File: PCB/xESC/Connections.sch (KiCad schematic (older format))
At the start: 1 part

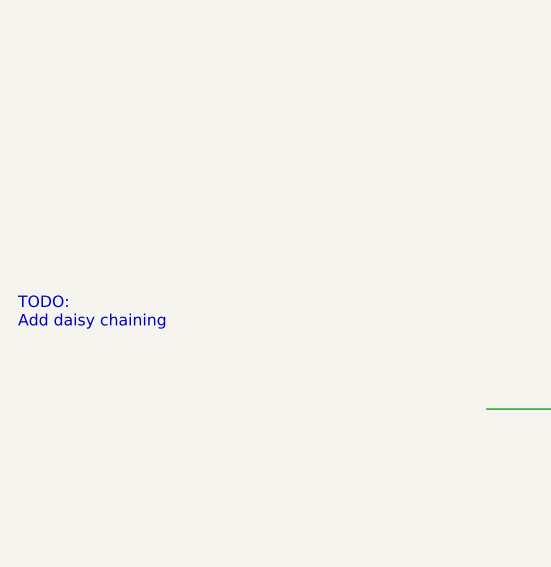
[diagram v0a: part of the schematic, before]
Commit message: added missing connection
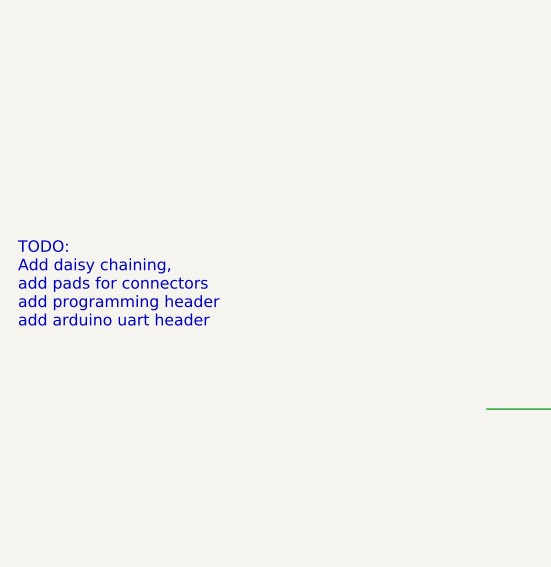
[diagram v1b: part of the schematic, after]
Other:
- note added: "TODO:\nAdd daisy chaining,\nadd pads for connectors\nadd programming header\nadd arduino uart header"
- note removed: "TODO:\nAdd daisy chaining"
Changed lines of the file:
@@
 RXD
 Text Notes 2100 3000 0    50   ~ 0
-TODO:\nAdd daisy chaining
+TODO:\nAdd daisy chaining,\nadd pads for connectors\nadd programming header\nadd arduino uart header
 Text HLabel 5750 3650 2    50   Output ~ 0
 INPUT

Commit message: wip
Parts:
- gave numbers to parts that had none: 1
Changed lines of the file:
@@
 VCCIO
 $Comp
-L Device:R R?
+L Device:R R16
 U 1 1 61826336
 P 5000 3200
-F 0 "R?" V 5207 3200 50  0000 C CNN
+F 0 "R16" V 5207 3200 50  0000 C CNN
 F 1 "1kR" V 5116 3200 50  0000 C CNN
 F 2 "Resistor_SMD:R_0805_2012Metric_Pad1.20x1.40mm_HandSolder" V 4930 3200 50  0001 C CNN

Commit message: wip
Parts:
- added J1: Conn_01x05_Male, Connector_PinHeader_2.54mm:PinHeader_1x05_P2.54mm_Vertical, symbol Connector:Conn_01x05_Male
- added J2, J3: Conn_01x03_Male, Connector_PinHeader_2.54mm:PinHeader_1x03_P2.54mm_Vertical, symbol Connector:Conn_01x03_Male
- added R? (x2): 1kR, Resistor_SMD:R_0805_2012Metric_Pad1.20x1.40mm_HandSolder, symbol Device:R
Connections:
- net labels added: INPUT_ANALOG, INPUT_PWM
- net labels removed: INPUT
- wire segments 3 -> 38
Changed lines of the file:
@@
 Text HLabel 5750 1800 2    50   UnSpc ~ 0
 GND
-Text HLabel 5750 2250 2    50   Input ~ 0
+Text HLabel 5750 2850 2    50   Input ~ 0
 HALL_V+
 Text HLabel 5750 2400 2    50   Output ~ 0
@@
 TODO:\nAdd daisy chaining,\nadd pads for connectors\nadd programming header\nadd arduino uart header
 Text HLabel 5750 3650 2    50   Output ~ 0
-INPUT
+INPUT_PWM
 Text HLabel 5750 4000 2    50   Input ~ 0
 U
@@
 Text HLabel 5750 5250 2    50   Input ~ 0
 SCK
+$Comp
+L Connector:Conn_01x05_Male J1
+U 1 1 61B78D2B
+P 4950 2450
+F 0 "J1" H 5058 2831 50  0000 C CNN
+F 1 "Conn_01x05_Male" H 5058 2740 50  0000 C CNN
+F 2 "Connector_PinHeader_2.54mm:PinHeader_1x05_P2.54mm_Vertical" H 4950 2450 50  0001 C CNN
+F 3 "~" H 4950 2450 50  0001 C CNN
+	1    4950 2450
+	1    0    0    -1
+$EndComp
+Wire Wire Line
+	5750 1800 5600 1800
+Wire Wire Line
+	5600 2250 5150 2250
+Wire Wire Line
+	5450 2400 5450 2350
+Wire Wire Line
+	5450 2350 5150 2350
+Wire Wire Line
+	5400 2550 5400 2450
+Wire Wire Line
+	5400 2450 5150 2450
+Wire Wire Line
+	5350 2700 5350 2550
+Wire Wire Line
+	5350 2550 5150 2550
+Wire Wire Line
+	5250 2850 5250 2650
+Wire Wire Line
+	5250 2650 5150 2650
+Wire Wire Line
+	5750 2850 5250 2850
+Wire Wire Line
+	5750 2700 5350 2700
+Wire Wire Line
+	5750 2550 5400 2550
+Wire Wire Line
+	5750 2400 5450 2400
+Wire Wire Line
+	5600 1800 5600 2250
+Text HLabel 5750 3750 2    50   Output ~ 0
+INPUT_ANALOG
+$Comp
+L Connector:Conn_01x03_Male J2
+U 1 1 61BD29C1
+P 3550 3750
+F 0 "J2" H 3658 4031 50  0000 C CNN
+F 1 "Conn_01x03_Male" H 3658 3940 50  0000 C CNN
+F 2 "Connector_PinHeader_2.54mm:PinHeader_1x03_P2.54mm_Vertical" H 3550 3750 50  0001 C CNN
+F 3 "~" H 3550 3750 50  0001 C CNN
+	1    3550 3750
+	1    0    0    -1
+$EndComp
+$Comp
+L Connector:Conn_01x03_Male J3
+U 1 1 61BD440A
+P 3550 4250
+F 0 "J3" H 3658 4531 50  0000 C CNN
+F 1 "Conn_01x03_Male" H 3658 4440 50  0000 C CNN
+F 2 "Connector_PinHeader_2.54mm:PinHeader_1x03_P2.54mm_Vertical" H 3550 4250 50  0001 C CNN
+F 3 "~" H 3550 4250 50  0001 C CNN
+	1    3550 4250
+	1    0    0    -1
+$EndComp
+$Comp
+L power:GND #PWR0117
+U 1 1 61BD4BA0
+P 5600 2250
+F 0 "#PWR0117" H 5600 2000 50  0001 C CNN
+F 1 "GND" H 5605 2077 50  0000 C CNN
+F 2 "" H 5600 2250 50  0001 C CNN
+F 3 "" H 5600 2250 50  0001 C CNN
+	1    5600 2250
+	1    0    0    -1
+$EndComp
+Connection ~ 5600 2250
+Wire Wire Line
+	3750 3650 3950 3650
+Wire Wire Line
+	3950 3650 3950 4150
+Wire Wire Line
+	3750 4150 3950 4150
+Connection ~ 3950 4150
+Wire Wire Line
+	3950 4150 3950 4650
+Wire Wire Line
+	3750 4250 4050 4250
+Wire Wire Line
+	4050 4250 4050 3750
+Wire Wire Line
+	3750 3750 4050 3750
+Connection ~ 4050 3750
+Wire Wire Line
+	5750 1500 4050 1500
+Wire Wire Line
+	4050 1500 4050 3750
+Wire Wire Line
+	3750 3850 5150 3850
+Wire Wire Line
+	5150 3850 5150 3650
+Wire Wire Line
+	5150 3650 5750 3650
+Wire Wire Line
+	5750 3750 5250 3750
+Wire Wire Line
+	5250 3750 5250 4150
+Wire Wire Line
+	5250 4350 3750 4350
+$Comp
+L power:GND #PWR0118
+U 1 1 61BD88B8
+P 3950 4650
+F 0 "#PWR0118" H 3950 4400 50  0001 C CNN
+F 1 "GND" H 3955 4477 50  0000 C CNN
+F 2 "" H 3950 4650 50  0001 C CNN
+F 3 "" H 3950 4650 50  0001 C CNN
+	1    3950 4650
+	1    0    0    -1
+$EndComp
+$Comp
+L Device:R R?
+U 1 1 61BF443C
+P 4900 3650
+F 0 "R?" V 5107 3650 50  0000 C CNN
+F 1 "1kR" V 5016 3650 50  0000 C CNN
+F 2 "Resistor_SMD:R_0805_2012Metric_Pad1.20x1.40mm_HandSolder" V 4830 3650 50  0001 C CNN
+F 3 "~" H 4900 3650 50  0001 C CNN
+	1    4900 3650
+	0    1    1    0
+$EndComp
+$Comp
+L Device:R R?
+U 1 1 61BF524C
+P 4900 4150
+F 0 "R?" V 5107 4150 50  0000 C CNN
+F 1 "1kR" V 5016 4150 50  0000 C CNN
+F 2 "Resistor_SMD:R_0805_2012Metric_Pad1.20x1.40mm_HandSolder" V 4830 4150 50  0001 C CNN
+F 3 "~" H 4900 4150 50  0001 C CNN
+	1    4900 4150
+	0    1    1    0
+$EndComp
+Wire Wire Line
+	5150 3650 5050 3650
+Connection ~ 5150 3650
+Wire Wire Line
+	5050 4150 5250 4150
+Connection ~ 5250 4150
+Wire Wire Line
+	5250 4150 5250 4350
+Wire Wire Line
+	4750 4150 3950 4150
+Wire Wire Line
+	4750 3650 3950 3650
+Connection ~ 3950 3650
 $EndSCHEMATC

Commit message: wip
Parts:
- added J4: Conn_01x03_Male, Connector_PinHeader_2.54mm:PinHeader_1x03_P2.54mm_Vertical, symbol Connector:Conn_01x03_Male
- added TP1, TP2, TP3, TP4, TP5, TP6, TP7, TP?: TestPoint, xESC:TestPoint_Pad_1.5x1.5mm, symbol Connector:TestPoint
- gave numbers to parts that had none: 2
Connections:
- net labels added: SS_EXT_SPI
- net labels removed: HALL_V+
- wire segments 38 -> 50
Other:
- note added: "Phase is connected using\nmanually placed solder pads"
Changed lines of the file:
@@
 Comment4 ""
 $EndDescr
-Text HLabel 5750 1650 2    50   Output ~ 0
+Text HLabel 7700 5400 2    50   Output ~ 0
 V_IN
 Text HLabel 5750 1800 2    50   UnSpc ~ 0
 GND
-Text HLabel 5750 2850 2    50   Input ~ 0
-HALL_V+
 Text HLabel 5750 2400 2    50   Output ~ 0
 HALL_U
@@
 Text HLabel 5750 3200 2    50   Input ~ 0
 TXD
-Text HLabel 5750 3350 2    50   Output ~ 0
-RXD
 Text Notes 2100 3000 0    50   ~ 0
 TODO:\nAdd daisy chaining,\nadd pads for connectors\nadd programming header\nadd arduino uart header
 Text HLabel 5750 3650 2    50   Output ~ 0
 INPUT_PWM
-Text HLabel 5750 4000 2    50   Input ~ 0
-U
-Text HLabel 5750 4150 2    50   Input ~ 0
-V
-Text HLabel 5750 4300 2    50   Input ~ 0
-W
 Text HLabel 5750 1500 2    50   Input ~ 0
 VCCIO
@@
 Wire Wire Line
 	4850 3200 4600 3200
-Wire Wire Line
-	4150 3350 5750 3350
-Text HLabel 5750 4750 2    50   Input ~ 0
+Text HLabel 4750 5800 2    50   Input ~ 0
 RESET
-Text HLabel 5750 4900 2    50   Input ~ 0
+Text HLabel 4750 5600 2    50   Input ~ 0
 MISO
-Text HLabel 5750 5050 2    50   Input ~ 0
+Text HLabel 4750 5700 2    50   Input ~ 0
 MOSI
-Text HLabel 5750 5250 2    50   Input ~ 0
+Text HLabel 4750 5500 2    50   Input ~ 0
 SCK
 $Comp
@@
 	5250 2650 5150 2650
 Wire Wire Line
-	5750 2850 5250 2850
-Wire Wire Line
 	5750 2700 5350 2700
 Wire Wire Line
@@
 Connection ~ 3950 4150
 Wire Wire Line
-	3950 4150 3950 4650
+	3950 4150 3950 4550
 Wire Wire Line
 	3750 4250 4050 4250
@@
 Wire Wire Line
 	3750 3750 4050 3750
-Connection ~ 4050 3750
-Wire Wire Line
-	5750 1500 4050 1500
-Wire Wire Line
-	4050 1500 4050 3750
 Wire Wire Line
 	3750 3850 5150 3850
@@
 $EndComp
 $Comp
-L Device:R R?
+L Device:R R17
 U 1 1 61BF443C
 P 4900 3650
-F 0 "R?" V 5107 3650 50  0000 C CNN
+F 0 "R17" V 5107 3650 50  0000 C CNN
 F 1 "1kR" V 5016 3650 50  0000 C CNN
 F 2 "Resistor_SMD:R_0805_2012Metric_Pad1.20x1.40mm_HandSolder" V 4830 3650 50  0001 C CNN
@@
 $EndComp
 $Comp
-L Device:R R?
+L Device:R R18
 U 1 1 61BF524C
 P 4900 4150
-F 0 "R?" V 5107 4150 50  0000 C CNN
+F 0 "R18" V 5107 4150 50  0000 C CNN
 F 1 "1kR" V 5016 4150 50  0000 C CNN
 F 2 "Resistor_SMD:R_0805_2012Metric_Pad1.20x1.40mm_HandSolder" V 4830 4150 50  0001 C CNN
@@
 	4750 3650 3950 3650
 Connection ~ 3950 3650
+Wire Wire Line
+	4550 1500 4550 2850
+Wire Wire Line
+	4550 2850 5250 2850
+Connection ~ 4550 1500
+Wire Wire Line
+	4550 1500 4050 1500
+Text HLabel 7700 5850 2    50   Input ~ 0
+W
+Text HLabel 7700 5700 2    50   Input ~ 0
+V
+Text HLabel 7700 5550 2    50   Input ~ 0
+U
+Text Notes 6550 5750 0    50   ~ 0
+Phase is connected using\nmanually placed solder pads
+$Comp
+L Connector:TestPoint TP2
+U 1 1 61D6B8CA
+P 4600 3200
+F 0 "TP2" H 4542 3226 50  0000 R CNN
+F 1 "TestPoint" H 4542 3317 50  0000 R CNN
+F 2 "xESC:TestPoint_Pad_1.5x1.5mm" H 4800 3200 50  0001 C CNN
+F 3 "~" H 4800 3200 50  0001 C CNN
+	1    4600 3200
+	-1   0    0    1
+$EndComp
+$Comp
+L Connector:TestPoint TP6
+U 1 1 61D6DCA6
+P 4500 5800
+F 0 "TP6" H 4558 5918 50  0000 L CNN
+F 1 "TestPoint" H 4558 5827 50  0000 L CNN
+F 2 "xESC:TestPoint_Pad_1.5x1.5mm" H 4700 5800 50  0001 C CNN
+F 3 "~" H 4700 5800 50  0001 C CNN
+	1    4500 5800
+	1    0    0    -1
+$EndComp
+$Comp
+L Connector:TestPoint TP5
+U 1 1 61D6E8CA
+P 4500 5600
+F 0 "TP5" H 4558 5718 50  0000 L CNN
+F 1 "TestPoint" H 4558 5627 50  0000 L CNN
+F 2 "xESC:TestPoint_Pad_1.5x1.5mm" H 4700 5600 50  0001 C CNN
+F 3 "~" H 4700 5600 50  0001 C CNN
+	1    4500 5600
+	1    0    0    -1
+$EndComp
+$Comp
+L Connector:TestPoint TP4
+U 1 1 61D6F700
+P 4400 5700
+F 0 "TP4" H 4458 5818 50  0000 L CNN
+F 1 "TestPoint" H 4458 5727 50  0000 L CNN
+F 2 "xESC:TestPoint_Pad_1.5x1.5mm" H 4600 5700 50  0001 C CNN
+F 3 "~" H 4600 5700 50  0001 C CNN
+	1    4400 5700
+	1    0    0    -1
+$EndComp
+$Comp
+L Connector:TestPoint TP3
+U 1 1 61D70C5B
+P 4400 5500
+F 0 "TP3" H 4458 5618 50  0000 L CNN
+F 1 "TestPoint" H 4458 5527 50  0000 L CNN
+F 2 "xESC:TestPoint_Pad_1.5x1.5mm" H 4600 5500 50  0001 C CNN
+F 3 "~" H 4600 5500 50  0001 C CNN
+	1    4400 5500
+	1    0    0    -1
+$EndComp
+Wire Wire Line
+	4750 5800 4500 5800
+Wire Wire Line
+	4500 5600 4750 5600
+Wire Wire Line
+	4750 5700 4400 5700
+Wire Wire Line
+	4400 5500 4750 5500
+$Comp
+L Connector:TestPoint TP7
+U 1 1 61D76261
+P 3950 4550
+F 0 "TP7" H 4008 4668 50  0000 L CNN
+F 1 "TestPoint" H 4008 4577 50  0000 L CNN
+F 2 "xESC:TestPoint_Pad_1.5x1.5mm" H 4150 4550 50  0001 C CNN
+F 3 "~" H 4150 4550 50  0001 C CNN
+	1    3950 4550
+	0    -1   -1   0
+$EndComp
+Connection ~ 3950 4550
+Wire Wire Line
+	3950 4550 3950 4650
+Wire Wire Line
+	4550 1500 5750 1500
+$Comp
+L Connector:Conn_01x03_Male J4
+U 1 1 61DB3B50
+P 3550 3100
+F 0 "J4" H 3658 3381 50  0000 C CNN
+F 1 "Conn_01x03_Male" H 3658 3290 50  0000 C CNN
+F 2 "Connector_PinHeader_2.54mm:PinHeader_1x03_P2.54mm_Vertical" H 3550 3100 50  0001 C CNN
+F 3 "~" H 3550 3100 50  0001 C CNN
+	1    3550 3100
+	1    0    0    -1
+$EndComp
+Connection ~ 4050 3750
+$Comp
+L Connector:TestPoint TP1
+U 1 1 61D6C509
+P 4150 3100
+F 0 "TP1" H 4208 3218 50  0000 L CNN
+F 1 "TestPoint" H 4208 3127 50  0000 L CNN
+F 2 "xESC:TestPoint_Pad_1.5x1.5mm" H 4350 3100 50  0001 C CNN
+F 3 "~" H 4350 3100 50  0001 C CNN
+	1    4150 3100
+	1    0    0    -1
+$EndComp
+Wire Wire Line
+	4050 1500 4050 3750
+Wire Wire Line
+	4150 3100 5750 3100
+Text HLabel 5750 3100 2    50   Output ~ 0
+RXD
+Wire Wire Line
+	4150 3100 3750 3100
+Connection ~ 4150 3100
+Wire Wire Line
+	4600 3200 3750 3200
+Connection ~ 4600 3200
+Wire Wire Line
+	3750 3000 3950 3000
+Wire Wire Line
+	3950 3000 3950 3650
+Text HLabel 4800 6100 2    50   Input ~ 0
+SS_EXT_SPI
+$Comp
+L Connector:TestPoint TP?
+U 1 1 61DD08D4
+P 4550 6100
+F 0 "TP?" H 4608 6218 50  0000 L CNN
+F 1 "TestPoint" H 4608 6127 50  0000 L CNN
+F 2 "xESC:TestPoint_Pad_1.5x1.5mm" H 4750 6100 50  0001 C CNN
+F 3 "~" H 4750 6100 50  0001 C CNN
+	1    4550 6100
+	1    0    0    -1
+$EndComp
+Wire Wire Line
+	4800 6100 4550 6100
 $EndSCHEMATC

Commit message: added logo, version and github link
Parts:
- added D2: D_Schottky, Diode_SMD:D_0805_2012Metric_Pad1.15x1.40mm_HandSolder, symbol Device:D_Schottky
- added TP9: TestPoint, xESC:TestPoint_Pad_1.5x1.5mm, symbol Connector:TestPoint
- gave numbers to parts that had none: 1
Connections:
- net VCCIO: now also D2.1 (K)
- new net: D2.2 (A), TP9.1
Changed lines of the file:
@@
 SS_EXT_SPI
 $Comp
-L Connector:TestPoint TP?
+L Connector:TestPoint TP8
 U 1 1 61DD08D4
 P 4550 6100
-F 0 "TP?" H 4608 6218 50  0000 L CNN
+F 0 "TP8" H 4608 6218 50  0000 L CNN
 F 1 "TestPoint" H 4608 6127 50  0000 L CNN
 F 2 "xESC:TestPoint_Pad_1.5x1.5mm" H 4750 6100 50  0001 C CNN
@@
 Wire Wire Line
 	4800 6100 4550 6100
+$Comp
+L Connector:TestPoint TP9
+U 1 1 61E1451D
+P 3400 1450
+F 0 "TP9" H 3458 1568 50  0000 L CNN
+F 1 "TestPoint" H 3458 1477 50  0000 L CNN
+F 2 "xESC:TestPoint_Pad_1.5x1.5mm" H 3600 1450 50  0001 C CNN
+F 3 "~" H 3600 1450 50  0001 C CNN
+	1    3400 1450
+	1    0    0    -1
+$EndComp
+$Comp
+L Device:D_Schottky D2
+U 1 1 61E15E2F
+P 3700 1500
+F 0 "D2" H 3700 1283 50  0000 C CNN
+F 1 "D_Schottky" H 3700 1374 50  0000 C CNN
+F 2 "Diode_SMD:D_0805_2012Metric_Pad1.15x1.40mm_HandSolder" H 3700 1500 50  0001 C CNN
+F 3 "~" H 3700 1500 50  0001 C CNN
+	1    3700 1500
+	-1   0    0    1
+$EndComp
+Wire Wire Line
+	4050 1500 3850 1500
+Connection ~ 4050 1500
+Wire Wire Line
+	3550 1500 3400 1500
+Wire Wire Line
+	3400 1500 3400 1450
 $EndSCHEMATC

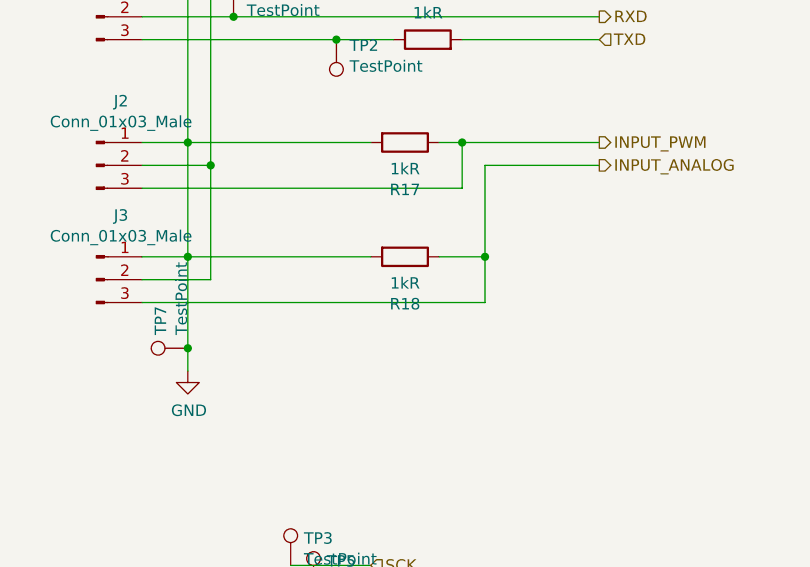
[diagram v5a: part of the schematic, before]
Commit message: Updated readme, changed analog pull down resistor to 10kR
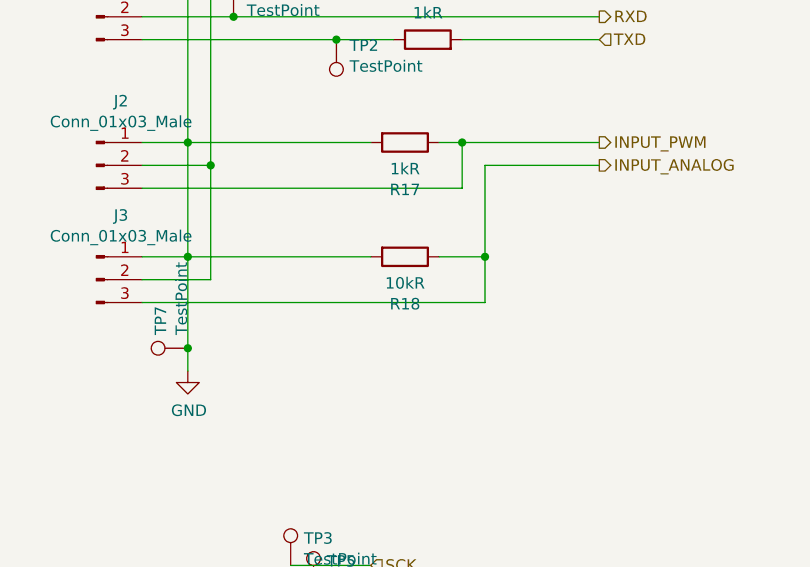
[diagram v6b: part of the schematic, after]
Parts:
- R18: value 1kR -> 10kR
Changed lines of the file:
@@
 P 4900 4150
 F 0 "R18" V 5107 4150 50  0000 C CNN
-F 1 "1kR" V 5016 4150 50  0000 C CNN
+F 1 "10kR" V 5016 4150 50  0000 C CNN
 F 2 "Resistor_SMD:R_0805_2012Metric_Pad1.20x1.40mm_HandSolder" V 4830 4150 50  0001 C CNN
 F 3 "~" H 4900 4150 50  0001 C CNN
